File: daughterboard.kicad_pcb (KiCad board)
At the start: 4 copper layers, 70 x 90 mm, 59 parts, among them J1 USB_OTG, J10 J, J11 J, J12 J, J13 J, J14 J, J15 J, J16 J, J17 J, J2 MotorA, J24 J, J25 J, J26 J, J27 J, J28 J, J29 J, J3 MotorB, J30 J, J31 J, J32 J, J33 QTR-8A, J34 J, J35 J, J4 BARREL_JACK, J5 Debug, J6 J, J7 J, SW1 Reset, U1 LD1117S33CTR, U2 TB6612FNG, U3 EFM32G230F128, Y1 Crystal

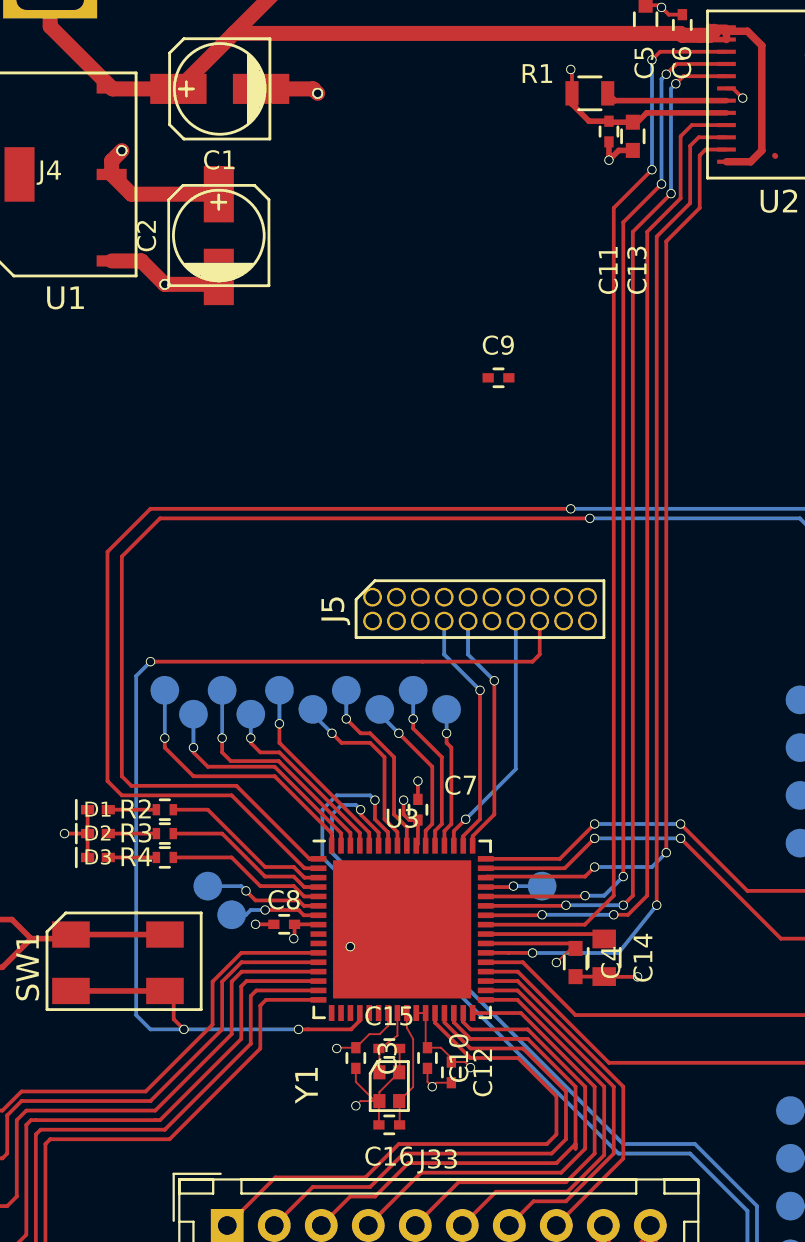
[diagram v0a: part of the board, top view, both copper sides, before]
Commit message: Finish routing
Could do with some cleanup, but it passes CRC.
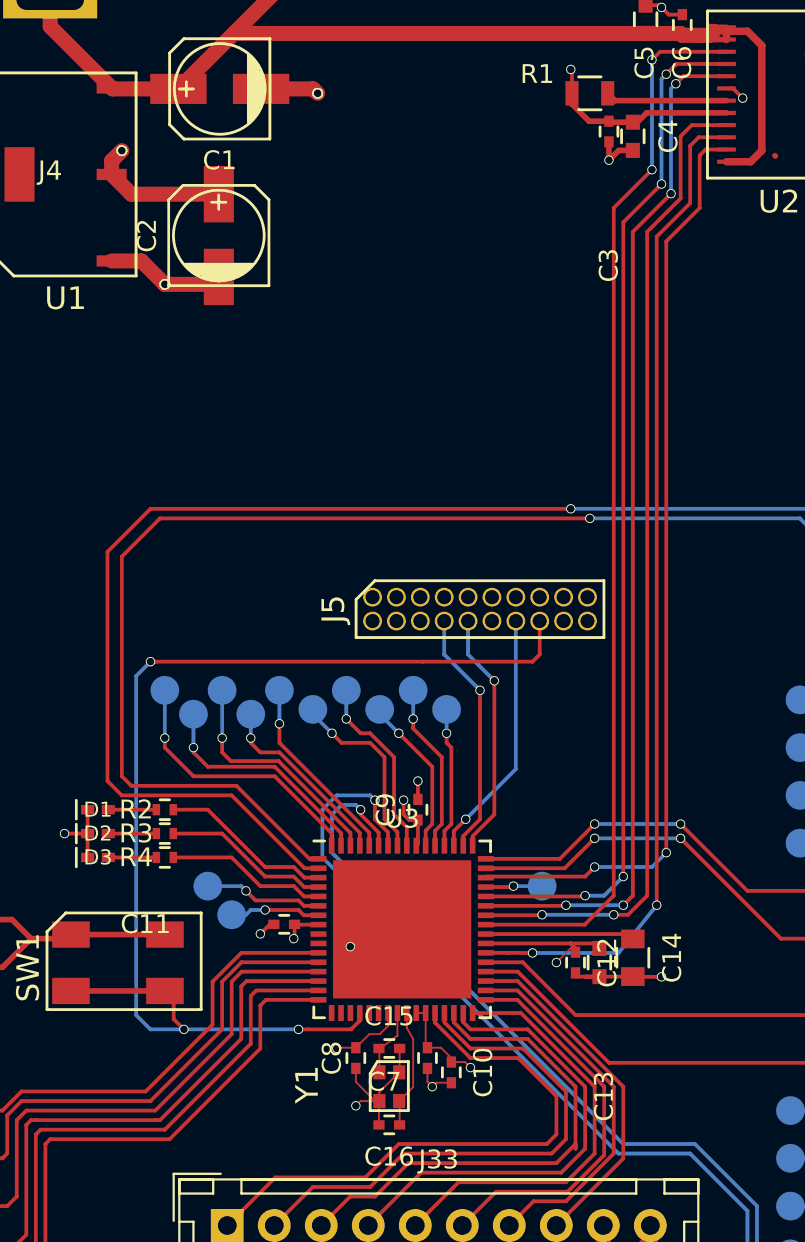
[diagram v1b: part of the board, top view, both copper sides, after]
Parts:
- moved C3 51.1 mm to (101.6, 80.5)
- moved C11 45.6 mm to (84.3, 122.7), turned to 180 degrees
- moved C4 44.0 mm to (102.9, 80.8)
- moved C13 44.0 mm to (101.1, 124.7)
- moved C9 23.4 mm to (91.4, 116.6), turned to 90 degrees
- moved C7 13.2 mm to (91.9, 129.8), turned to 270 degrees
- moved C12 8.82 mm to (99.8, 124.7)
- moved C8 8.07 mm to (88.1, 129.8), turned to 270 degrees
- moved C14 1.52 mm to (102.9, 124.5)
- moved C10 1.48 mm to (93.2, 130.6)
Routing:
- net GND: track 92.3 -> 94.5 mm
- net +3V3: track 56.8 -> 58.5 mm
- net /EFM32/DCPL: track 6.40 -> 7.93 mm

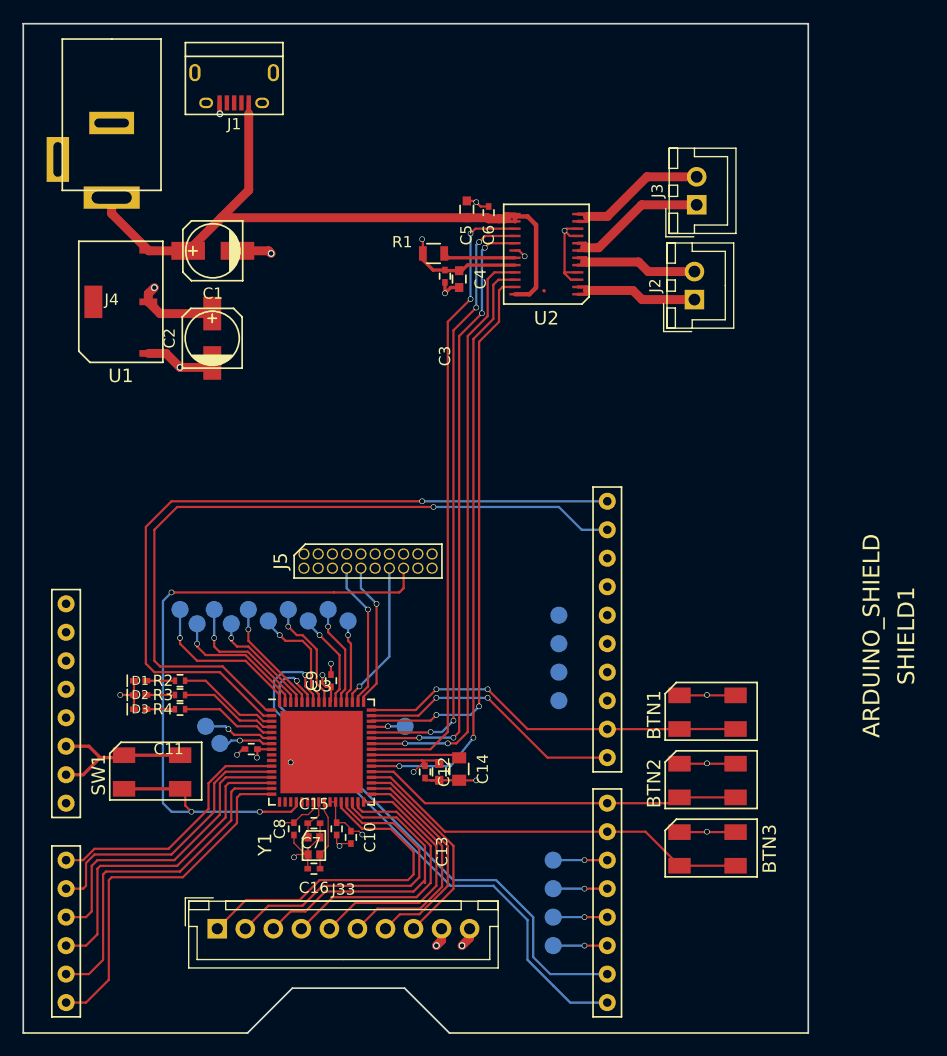
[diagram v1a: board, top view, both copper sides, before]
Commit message: Add logo
Also update footprint for barrel jack
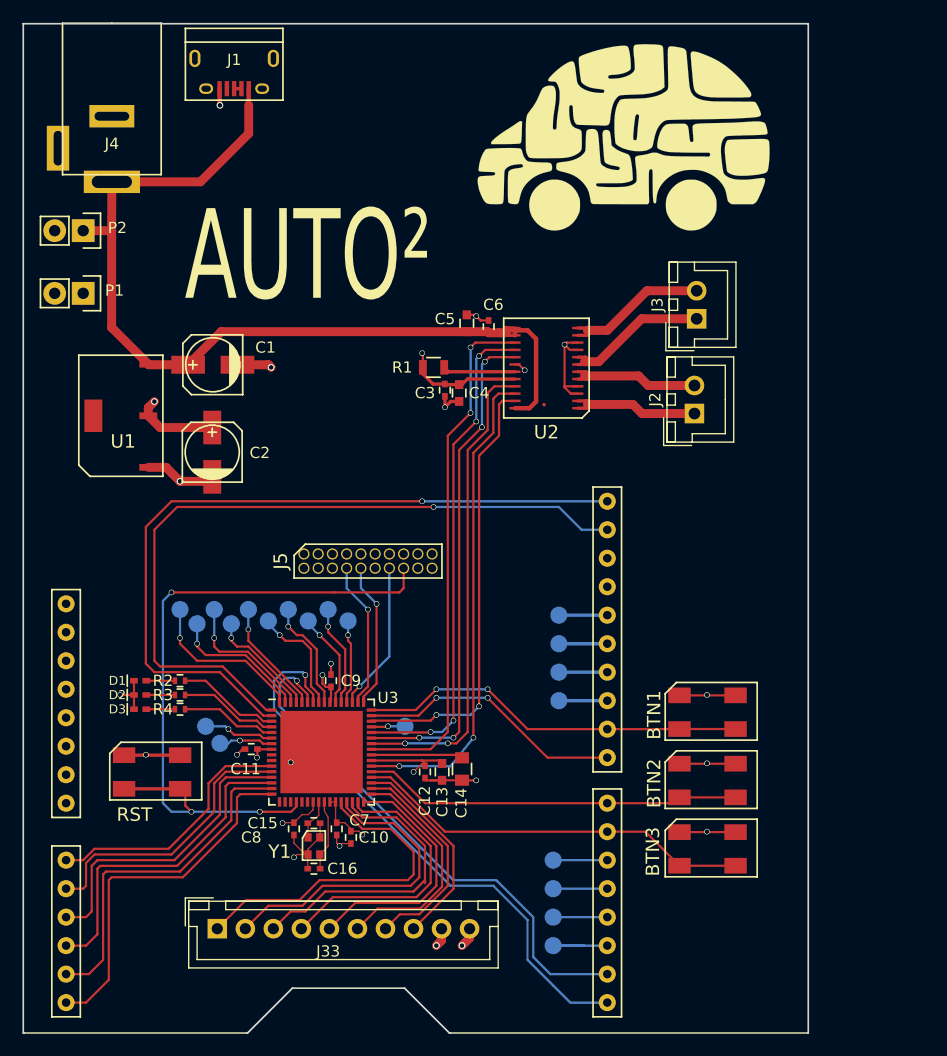
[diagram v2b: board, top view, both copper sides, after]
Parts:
- added G***: LOGO, lib_fp:logo, F.Cu at (118.0, 68.0)
- added P1: CONN_01X02, Pin_Headers:Pin_Header_Straight_1x02, F.Cu at (69.3, 82.0)
- added P2: CONN_01X02, Pin_Headers:Pin_Header_Straight_1x02, F.Cu at (69.3, 76.5)
- J4: footprint footprints:2.1-MM-DC-PWR -> lib_fp:Barrel
- moved C6 10.2 mm to (105.5, 85.0)
- moved J2 10.2 mm to (123.8, 92.8)
- moved C1 10.2 mm to (80.9, 88.4)
- moved C2 10.2 mm to (80.8, 96.2)
- moved C3 10.2 mm to (101.6, 90.7)
- moved C4 10.2 mm to (102.9, 90.9)
- moved C5 10.2 mm to (103.5, 84.7)
- moved J3 10.2 mm to (124.0, 84.3)
- moved R1 10.2 mm to (100.6, 88.6)
- moved U1 10.2 mm to (72.7, 93.0)
- moved U2 10.2 mm to (110.7, 88.7)
- moved J4 1.40 mm to (71.9, 68.7)
- moved J1 1.27 mm to (82.8, 62.2)
- moved C13 0.25 mm to (101.3, 124.7)
- moved C14 0.25 mm to (103.1, 124.5)
- renumbered SW1 to RST
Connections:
- J1 pad 3: Net-(J1-Pad3) -> Net-(J1-Pad2)
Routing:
- net +5V: track 63.9 -> 84.8 mm
- net /EFM32/AIN1: track 52.8 -> 42.7 mm
- net /EFM32/PWMB: track 56.9 -> 46.7 mm
- net /EFM32/PWMA: track 49.5 -> 39.4 mm
- net /EFM32/BIN2: track 54.8 -> 44.6 mm
- net /EFM32/AIN2: track 53.6 -> 43.4 mm
- net /EFM32/BIN1: track 55.0 -> 44.9 mm
- net GND: track 94.5 -> 86.8 mm, vias 15 -> 16
- net Net-(J15-Pad1): track 0.00 -> 4.32 mm
- net Net-(J14-Pad1): track 0.00 -> 4.32 mm
- net Net-(J13-Pad1): track 0.00 -> 4.32 mm
- net Net-(J12-Pad1): track 0.00 -> 4.32 mm
- net Net-(J10-Pad1): track 4.83 -> 7.62 mm, vias 1 -> 0
- net Net-(J1-Pad2): track 0.00 -> 0.65 mm
- net Net-(J17-Pad1): vias 1 -> 0
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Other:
- board text added: "AUTO²"
